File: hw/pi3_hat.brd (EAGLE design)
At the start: 56.5 x 65 mm, 116 parts, among them J1 XT30P, J2 XT30P, U1 AP64351SO8EP, U10 CAT24C32SOIC8, U11 STM32G474CEU6, U12 TCAN334GSOT23, U13 TCAN334GSOT23, U2 DMMT5401, U3 DMG2305UX, U4 STM32G474CEU6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

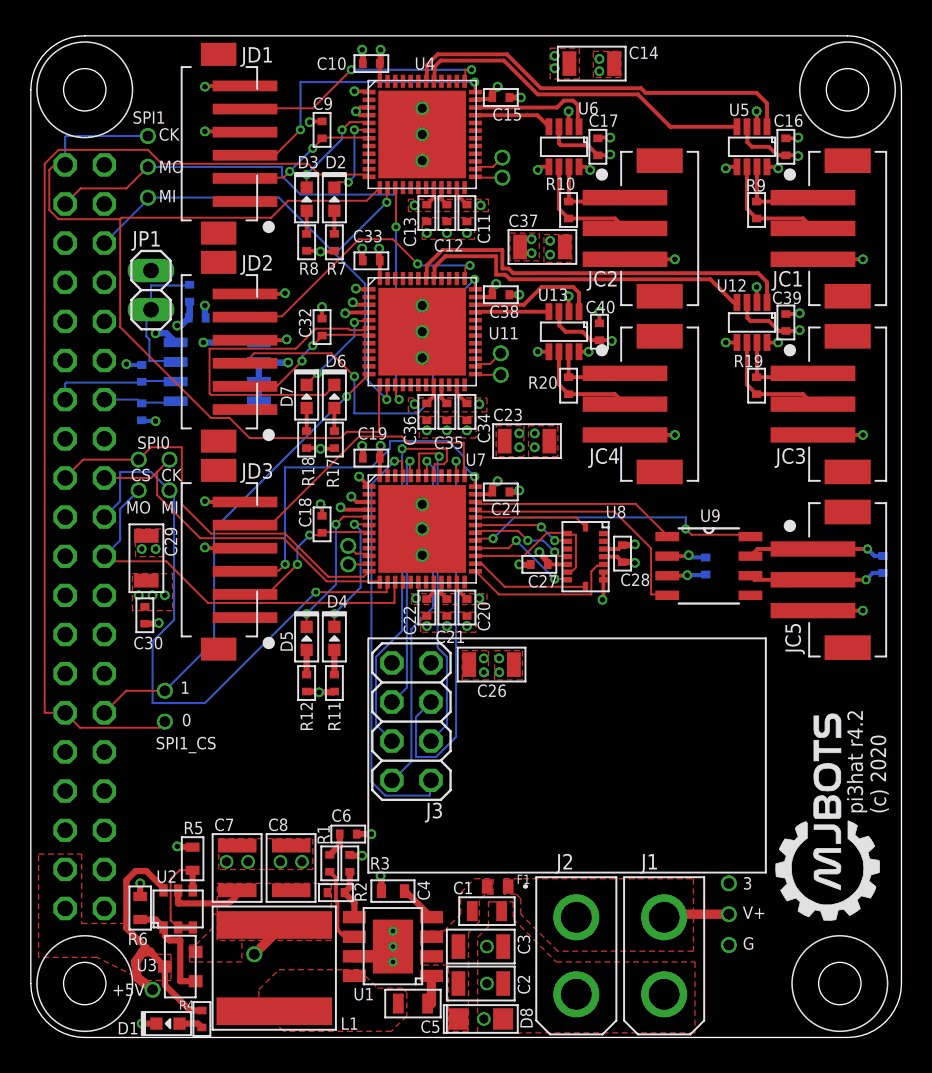
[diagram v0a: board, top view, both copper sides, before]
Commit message: Add IRQ lines to the rpi
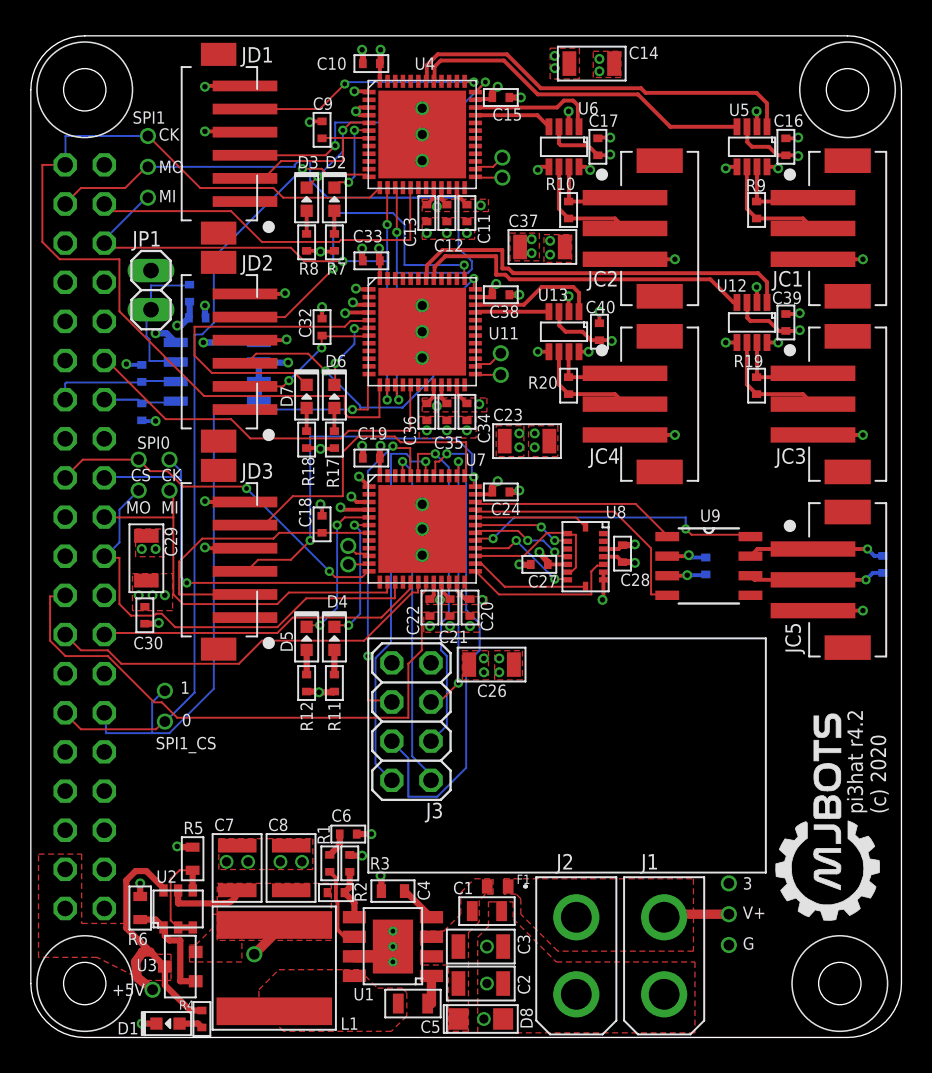
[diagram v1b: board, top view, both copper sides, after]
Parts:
- moved C20 0.20 mm to (28.5, 27.9)
- moved C21 0.20 mm to (27.2, 27.9)
- moved C22 0.20 mm to (25.9, 27.9)
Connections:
- new net AUX_IRQ1: J4.15, U7.17
- new net AUX_IRQ2: J4.16, U7.18
- new net AUX_IRQ3: J4.18, U7.19
- new net IFACEA_IRQ1: J4.37, U4.17
- new net IFACEB_IRQ1: J4.29, U11.17
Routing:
- net AUX_IRQ3: track 0.00 -> 38.5 mm
- net AUX_IRQ2: track 0.00 -> 26.3 mm
- net IFACEB_IRQ1: track 0.00 -> 25.1 mm
- net IFACEA_IRQ1: track 0.00 -> 24.3 mm
- net AUX_IRQ1: track 0.00 -> 21.5 mm
- net N$38: track 22.3 -> 5.16 mm, vias 0 -> 2
- net N$36: track 6.35 -> 21.4 mm, vias 2 -> 0
- net SPI1_CS0: track 66.1 -> 51.6 mm, vias 0 -> 1
- net SPI0_MISO: track 40.4 -> 26.6 mm, vias 1 -> 0
- net SPI1_MOSI: track 40.7 -> 53.5 mm
- net SPI1_CS1: track 30.6 -> 43.2 mm
- net N$47: track 10.5 -> 19.5 mm, vias 2 -> 0
- net NRF_CS: track 26.0 -> 17.7 mm, vias 1 -> 2
- net NRF_SCK: track 25.4 -> 32.9 mm
- net NRF_IRQ: track 28.1 -> 22.4 mm
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
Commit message: Expose debug pins on 0.1" headers, give 4 debug pins on the aux processor
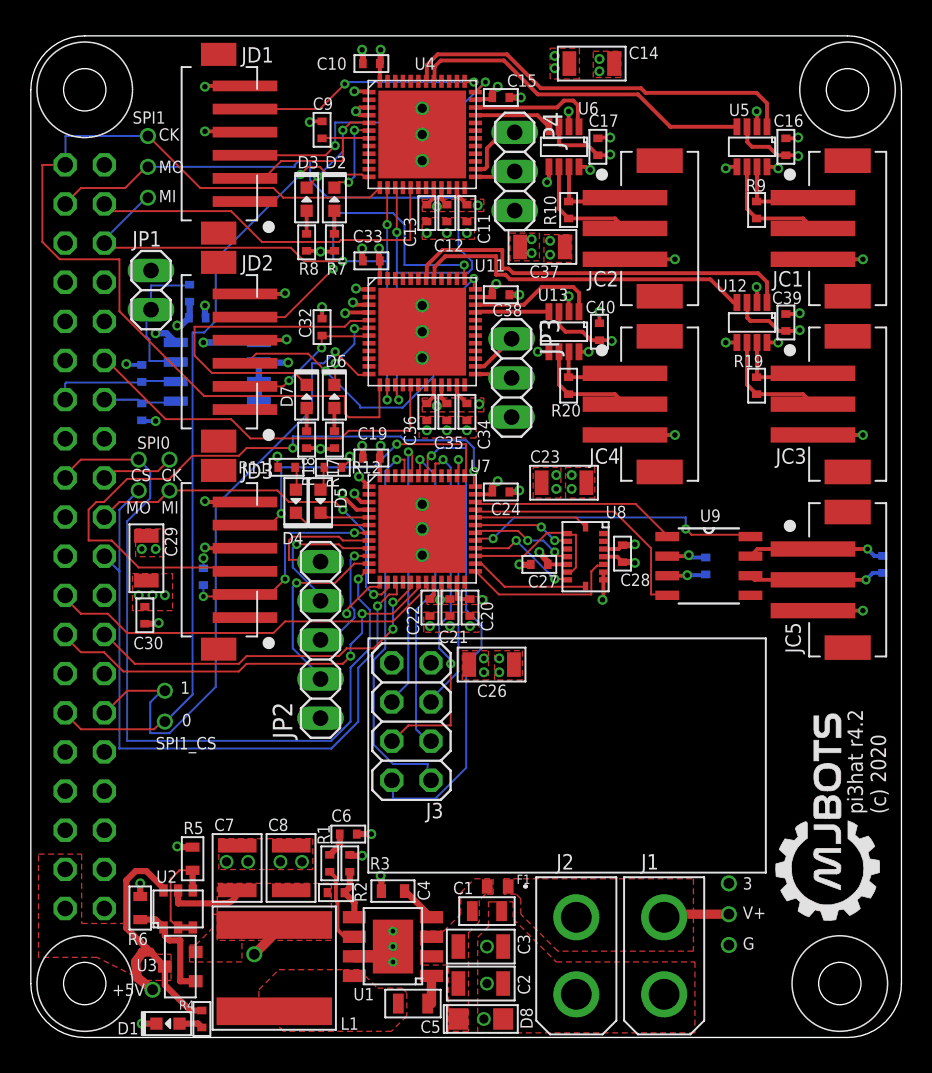
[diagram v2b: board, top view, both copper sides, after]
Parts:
- removed DBG1A, DBG1B, DBG2A, DBG2B, DBG3A, DBG3B: PAD24AWG_PAD, pi3_hat:24AWG_PAD
- added JP2: (no value), pinhead:1X05
- added JP3, JP4: (no value), pinhead:1X03
- moved R11 14.3 mm to (16.6, 37.0), turned to 0 degrees
- moved R12 14.1 mm to (19.6, 37.0), turned to 180 degrees
- moved D4 9.24 mm to (17.2, 34.8), turned to 90 degrees
- moved D5 8.95 mm to (18.8, 34.8), turned to 90 degrees
- moved C18 8.42 mm to (11.2, 29.9), flipped to the bottom
- moved C23 3.61 mm to (34.6, 36.0)
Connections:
- removed net DBG1A: DBG1A.P$1, U4.26
- removed net DBG1B: DBG1B.P$1, U4.25
- removed net DBG2A: DBG2A.P$1, U11.26
- removed net DBG2B: DBG2B.P$1, U11.25
- removed net DBG3A: DBG3A.P$1, U7.10
- removed net DBG3B: DBG3B.P$1, U7.11
- new net N$10: JP2.3, U7.10
- new net N$12: JP2.4, U7.9
- new net N$20: JP2.5, U7.8
- new net N$3: JP3.2, U11.25
- new net N$43: JP3.1, U11.26
- new net N$57: JP4.2, U4.25
- new net N$58: JP4.1, U4.26
- new net N$6: JP2.2, U7.11
- net GND: now also JP2.1, JP3.3, JP4.3
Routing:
- net SPI0_CS0: track 23.5 -> 50.5 mm, vias 2 -> 1
- net N$48: track 25.0 -> 43.3 mm
- net SPI0_MOSI: track 29.7 -> 45.3 mm, vias 0 -> 1
- net N$6: track 0.00 -> 12.3 mm, vias 0 -> 1
- net AUX_IRQ3: track 38.5 -> 26.4 mm
- net N$12: track 0.00 -> 9.30 mm, vias 0 -> 1
- net NRF_SCK: track 32.9 -> 23.8 mm, vias 1 -> 2
- net N$20: track 0.00 -> 8.79 mm
- net N$10: track 0.00 -> 7.96 mm, vias 0 -> 1
- net N$51: track 10.1 -> 3.26 mm, vias 2 -> 0
- net NRF_MISO: track 25.6 -> 32.4 mm
- net N$47: track 19.5 -> 14.9 mm, vias 0 -> 3
- net N$58: track 0.00 -> 4.24 mm
- net N$53: track 8.90 -> 5.08 mm, vias 2 -> 0
- net NRF_IRQ: track 22.4 -> 26.0 mm
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
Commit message: Stick two rpi pins on a header and fix silks
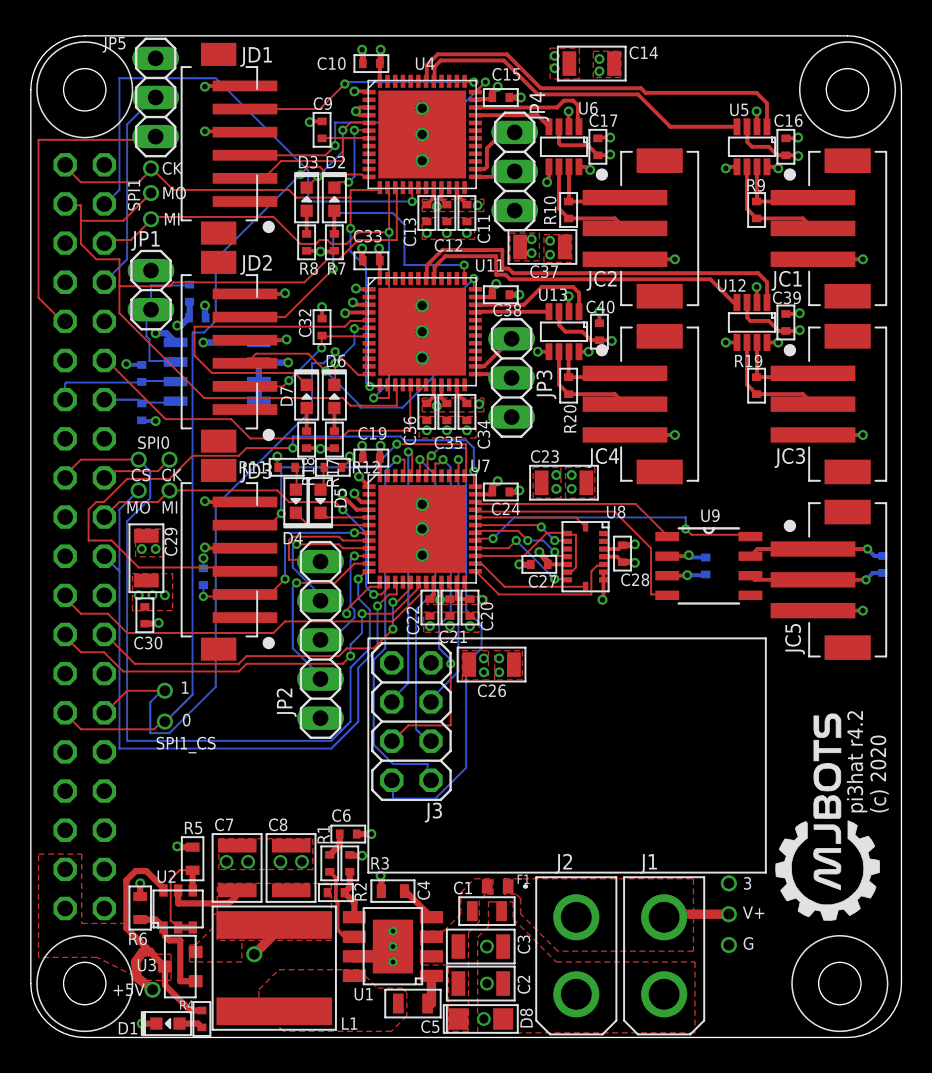
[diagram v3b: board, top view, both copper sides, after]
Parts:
- added JP5: (no value), pinhead:1X03
- moved SPI1_SCLK 2.11 mm to (7.80, 56.4)
- moved SPI1_MOSI 1.71 mm to (7.80, 54.8)
- moved SPI1_MISO 1.41 mm to (7.80, 53.1)
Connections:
- new net PI32: J4.32, JP5.1
- new net PI33: J4.33, JP5.2
- net GND: now also JP5.3
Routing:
- net SPI1_SCLK: track 62.0 -> 36.6 mm, vias 0 -> 2
- net PI32: track 0.00 -> 20.3 mm
- net PI33: track 0.00 -> 13.4 mm
- net IFACEA_IRQ1: track 24.3 -> 33.0 mm, vias 0 -> 1
- net SPI1_MOSI: track 53.5 -> 59.9 mm, vias 2 -> 0
- net SPI1_MISO: track 37.8 -> 36.4 mm, vias 3 -> 2

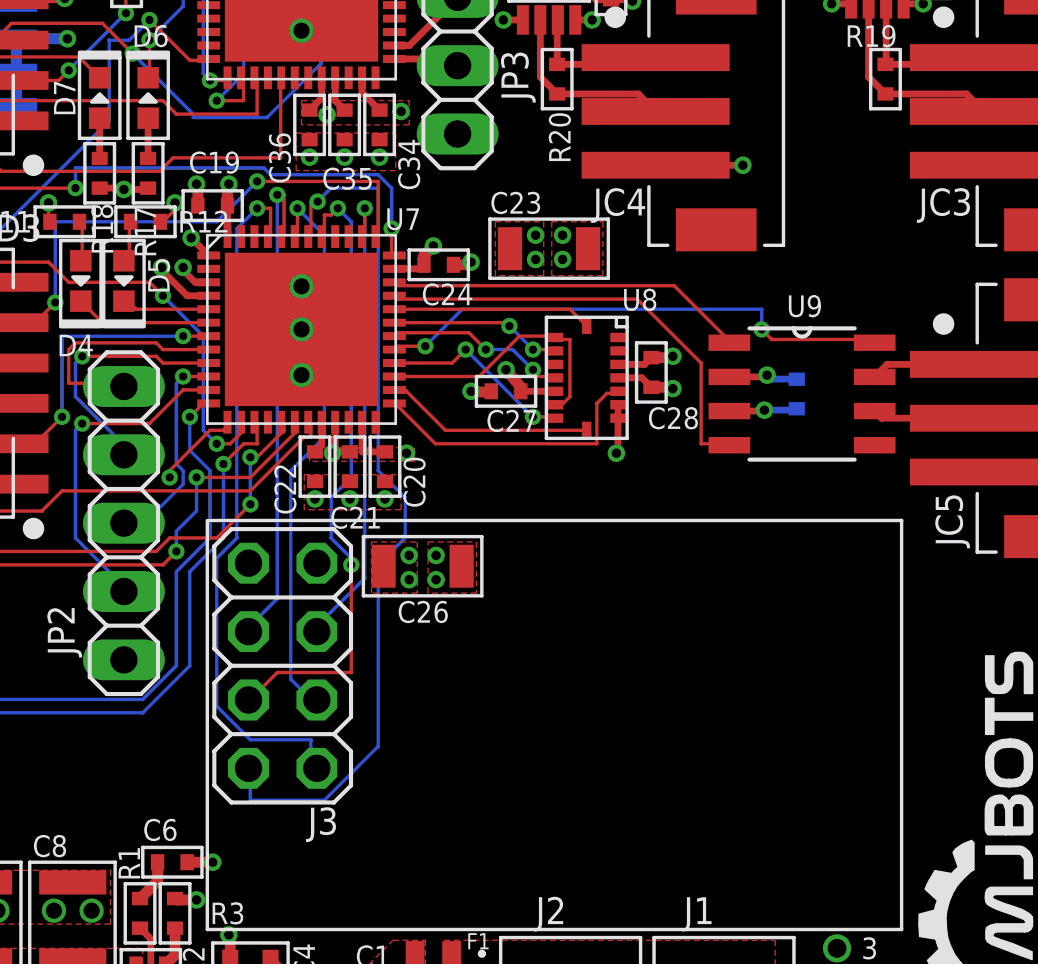
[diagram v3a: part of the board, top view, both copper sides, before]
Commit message: Add microphone to aux processor
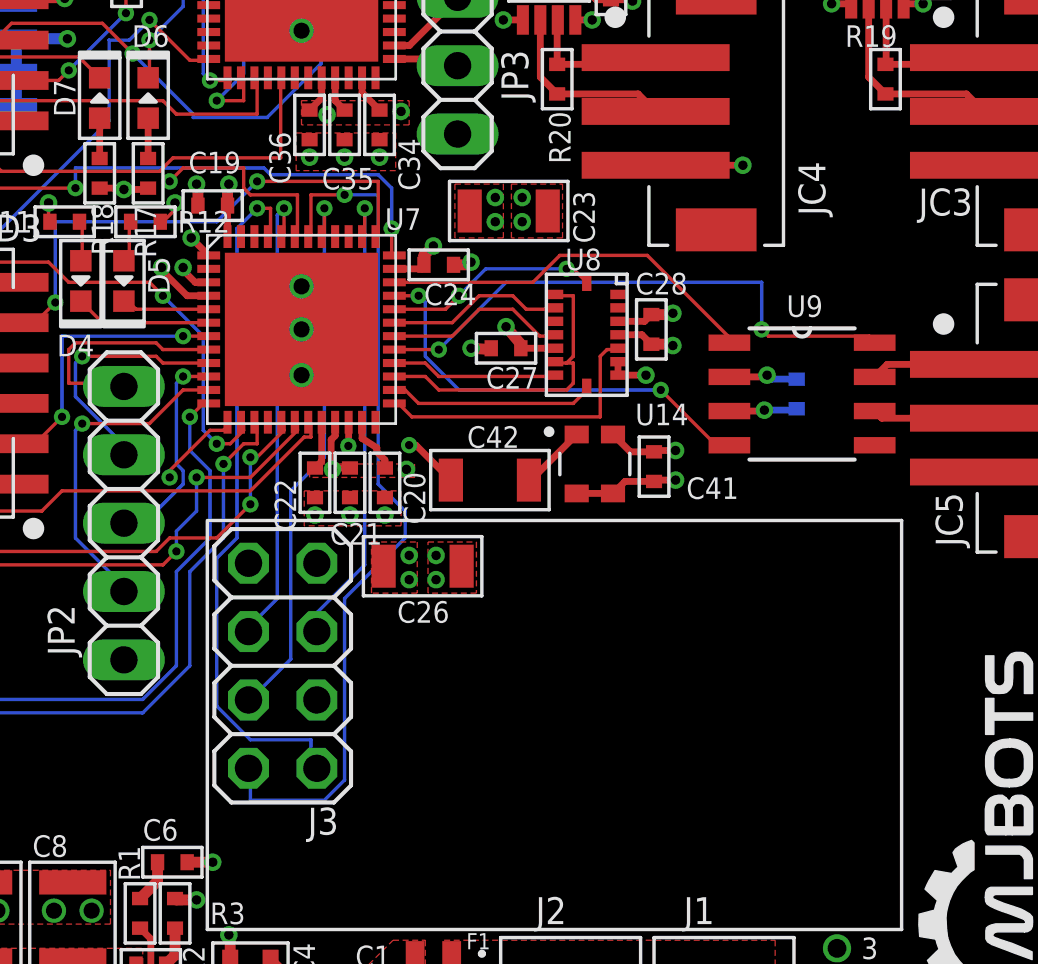
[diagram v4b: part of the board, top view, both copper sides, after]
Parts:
- added C41: 0.1uF, mfpassives:C0402
- added C42: 10uF, mfpassives:C1206
- added U14: SPW2430HR5H-B, SPW2430HR5H-B:MIC_SPW2430HR5H-B
- moved C23 2.05 mm to (33.1, 37.4)
- moved C28 1.60 mm to (38.4, 33.0)
- moved C27 1.60 mm to (33.0, 32.3)
- moved U8 1.60 mm to (36.0, 32.8)
- moved C20 0.60 mm to (28.5, 27.3)
- moved C21 0.60 mm to (27.2, 27.3)
- moved C22 0.60 mm to (25.9, 27.3)
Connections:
- new net MIC_IN: C42.P$2, U7.22
- new net N$59: C42.P$1, U14.1
- net +3V3: now also C41.P$1, U14.4
- net GND: now also C41.P$2, U14.2, U14.3
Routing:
- net NRF_MOSI: track 20.8 -> 30.3 mm
- net MIC_IN: track 0.00 -> 5.25 mm, vias 0 -> 2
- net +3V3: track 75.4 -> 79.5 mm, vias 46 -> 47
- net GND: track 75.7 -> 79.3 mm, vias 85 -> 86
- net NRF_SCK: track 23.8 -> 20.6 mm, vias 2 -> 1
- net N$59: track 0.00 -> 2.48 mm
- net IMU_MISO: track 10.00 -> 11.6 mm
- net CAN_SHDN: track 19.4 -> 20.9 mm
- net NRF_CE: track 18.5 -> 17.4 mm
- net IMU_MOSI: track 7.25 -> 6.21 mm, vias 2 -> 0
- net N$55: track 13.4 -> 14.3 mm
- net IMU_ACC_INT: track 7.42 -> 8.01 mm, vias 0 -> 2
- net N$54: track 16.5 -> 15.9 mm, vias 0 -> 2
- net IMU_CS1: track 6.42 -> 6.62 mm, vias 2 -> 0
- net IMU_GYRO_INT: track 6.73 -> 6.83 mm, vias 2 -> 0

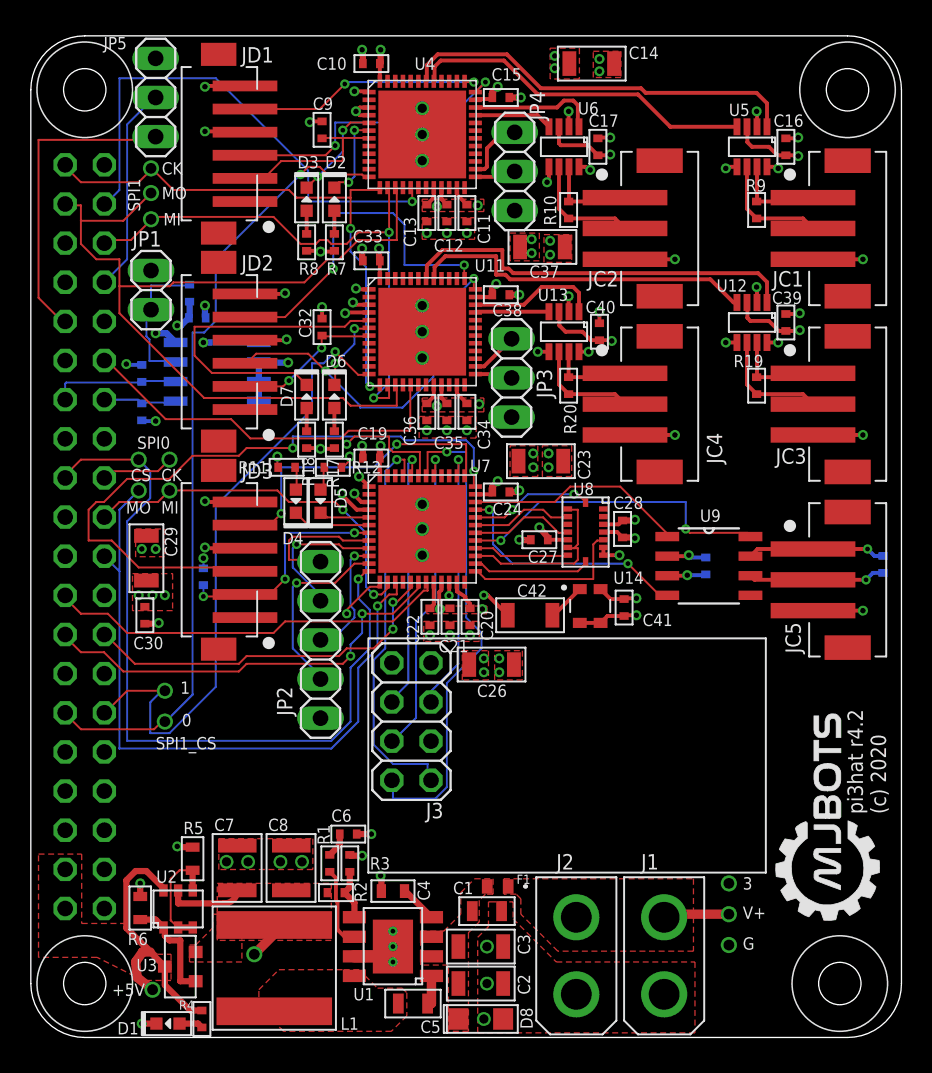
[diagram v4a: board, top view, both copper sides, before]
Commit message: Flip NRF around, add an LC filter and a ground plane
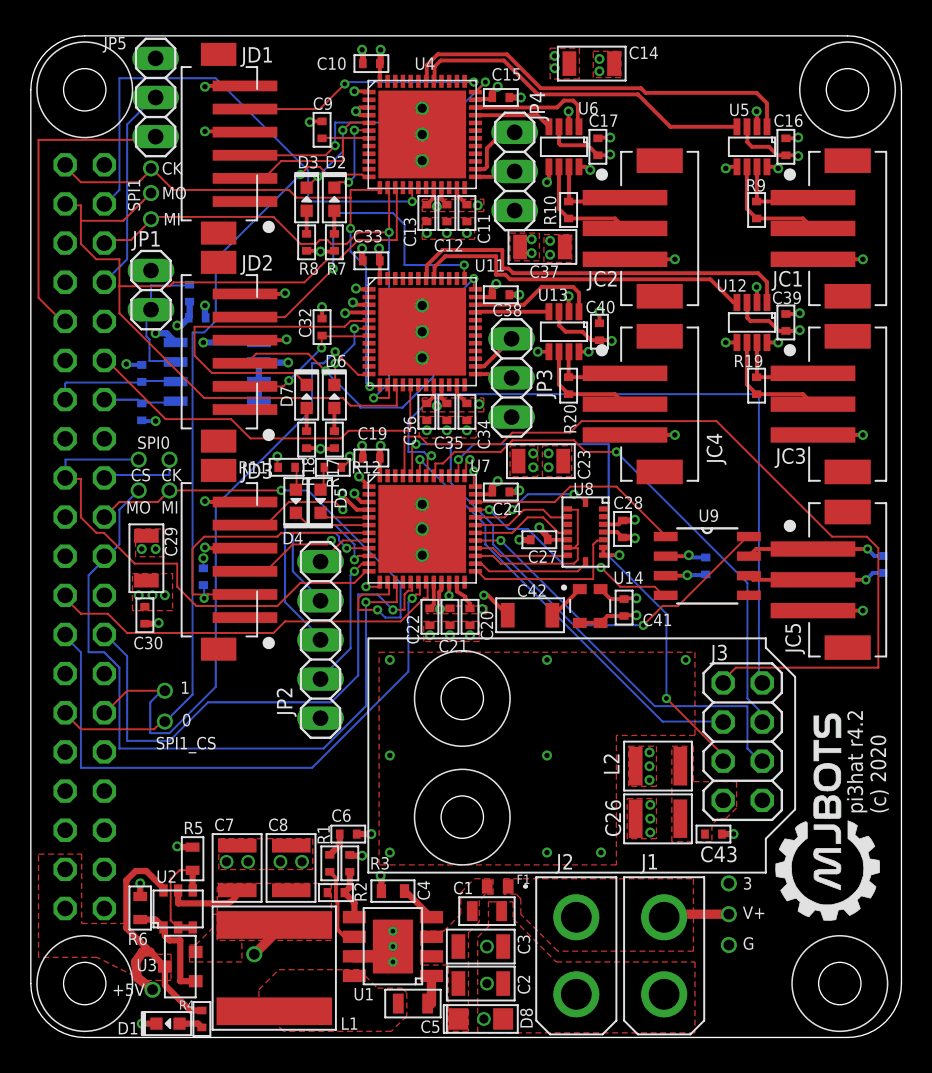
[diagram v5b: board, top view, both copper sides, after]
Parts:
- added C43: 0.1uF, mfpassives:C0402
- added L2: 10uH, mfpassives:L1210
- C26: value 10uF -> 22uF 16V; device mfpassives:C1206 -> mfpassives:C1210
- moved J3 21.5 mm to (46.2, 19.2), turned to 270 degrees
- moved C26 14.7 mm to (40.7, 14.2), turned to 180 degrees
- moved U9 0.10 mm to (43.9, 30.6)
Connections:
- new net N$56: C26.P$1, C43.P$1, J3.7, L2.P$2
- net +3V3: now also L2.P$1; no longer C26.P$1, J3.7
- net GND: now also C43.P$2
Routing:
- net NRF_IRQ: track 26.0 -> 55.9 mm, vias 1 -> 0
- net N$48: track 43.3 -> 18.8 mm
- net NRF_CE: track 17.4 -> 37.1 mm
- net SPI0_CS0: track 50.5 -> 32.4 mm, vias 1 -> 0
- net NRF_CS: track 17.6 -> 35.0 mm, vias 1 -> 2
- net NRF_MISO: track 32.2 -> 47.5 mm
- net NRF_SCK: track 20.6 -> 35.1 mm
- net AUX_IRQ2: track 27.9 -> 39.2 mm, vias 2 -> 1
- net AUX_IRQ1: track 24.2 -> 35.2 mm, vias 2 -> 1
- net N$10: track 7.96 -> 15.5 mm
- net SPI0_MISO: track 24.6 -> 31.4 mm
- net N$20: track 8.79 -> 3.70 mm
- net N$47: track 14.9 -> 19.5 mm, vias 3 -> 1
- net N$6: track 12.3 -> 9.05 mm
- net NRF_MOSI: track 30.3 -> 28.6 mm
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- added copper zone on layer 1, net N$56
